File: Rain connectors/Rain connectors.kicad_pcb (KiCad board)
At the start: 2 copper layers, 22.7 x 25 mm, 8 parts, among them J1 Conn_01x06_Socket, J2 Conn_01x06_Socket, J3 Conn_01x03_Socket

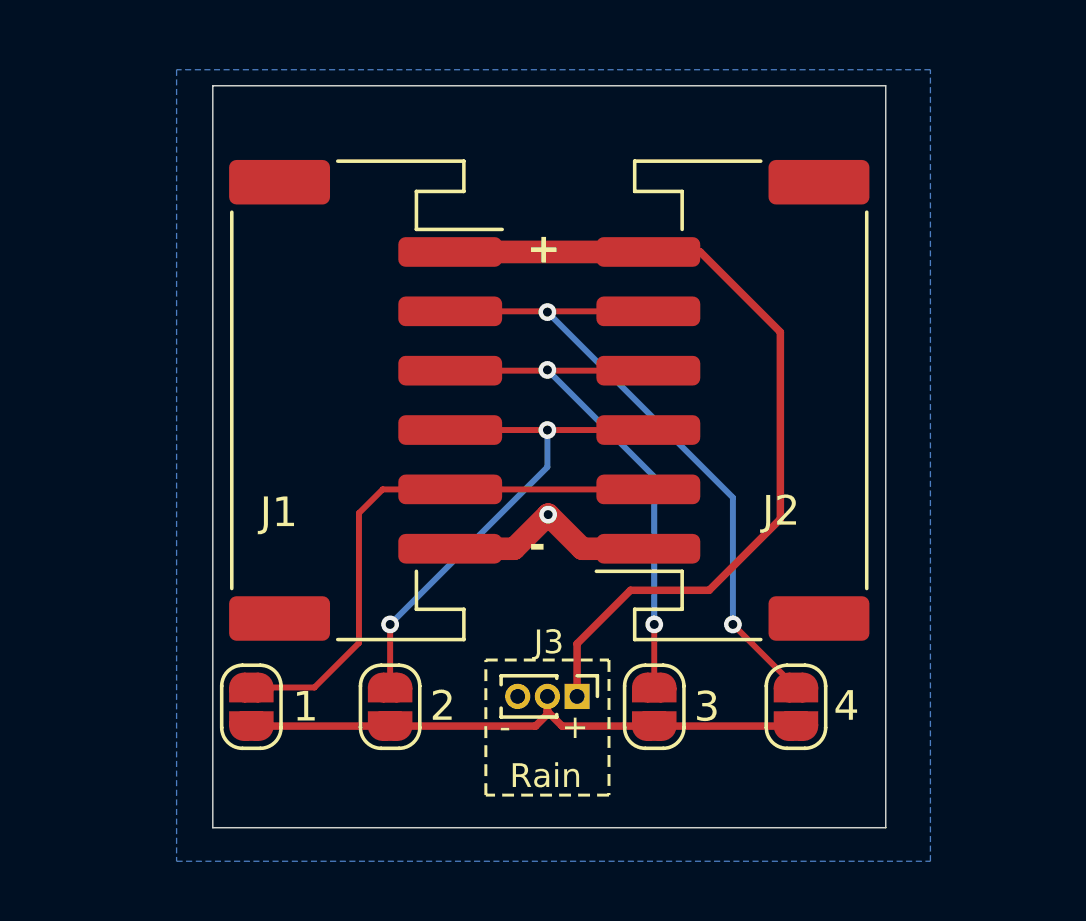
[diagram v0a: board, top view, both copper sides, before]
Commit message: Check to see if the rain connectors v.2. needs updating
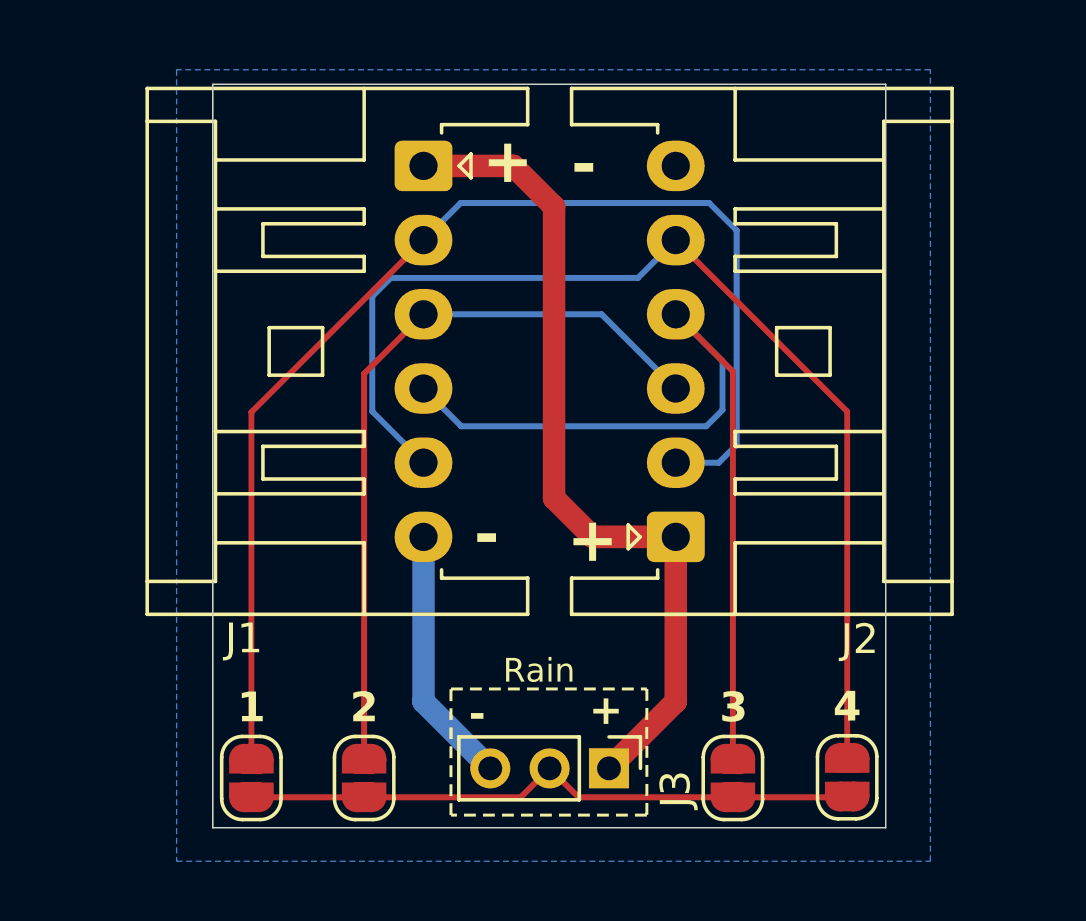
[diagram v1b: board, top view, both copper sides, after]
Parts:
- J1, J2: footprint Connector_JST:JST_PH_S6B-PH-SM4-TB_1x06-1MP_P2.00mm_Horizontal -> Connector_JST:JST_XA_S06B-XASK-1N-BN_1x06_P2.50mm_Horizontal
- J3: footprint Connector_PinHeader_1.00mm:PinHeader_1x03_P1.00mm_Vertical -> Connector_PinHeader_2.00mm:PinHeader_1x03_P2.00mm_Vertical
- moved J1 8.14 mm to (130.1, 74.2)
- moved J2 4.99 mm to (138.6, 86.7)
- moved REF** 4.93 mm to (134.4, 83.2)
- moved 3 3.58 mm to (140.5, 94.8)
- moved 4 2.94 mm to (144.4, 94.8)
- moved J3 2.65 mm to (136.3, 94.5)
- moved 2 2.55 mm to (128.1, 94.8)
- moved 1 2.40 mm to (124.3, 94.8)
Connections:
- 1 pad 2: Net-(J1-Pin_5) -> Net-(J1-Pin_2)
- 2 pad 2: Net-(J1-Pin_4) -> Net-(J1-Pin_3)
- 3 pad 2: Net-(J1-Pin_3) -> Net-(J1-Pin_4)
- 4 pad 2: Net-(J1-Pin_2) -> Net-(J1-Pin_5)
- J2 pad 1: GND -> +5V
- J2 pad 2: Net-(J1-Pin_5) -> Net-(J1-Pin_2)
- J2 pad 3: Net-(J1-Pin_4) -> Net-(J1-Pin_3)
- J2 pad 4: Net-(J1-Pin_3) -> Net-(J1-Pin_4)
- J2 pad 5: Net-(J1-Pin_2) -> Net-(J1-Pin_5)
- J2 pad 6: +5V -> GND
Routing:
- net Net-(J1-Pin_5): track 18.7 -> 37.2 mm
- net Net-(J1-Pin_2): track 22.8 -> 40.9 mm, vias 2 -> 0
- net Net-(J1-Pin_4): track 17.5 -> 30.5 mm, vias 2 -> 0
- net Net-(J1-Pin_3): track 18.9 -> 25.3 mm, vias 2 -> 0
- net GND: track 7.63 -> 8.73 mm, vias 1 -> 0
- net Net-(J3-Pin_2): track 19.9 -> 20.9 mm
- net +5V: track 28.9 -> 28.2 mm
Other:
- board text added: "330_Combined Sewer Tunnel Individual Rain Breakout Rev.2"
- board text removed: "330_Combined Sewer Tunnel Individual Rain Breakout Rev.1"

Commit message: Rev. 3
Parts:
- J1, J2: footprint Connector_JST:JST_XA_S06B-XASK-1N-BN_1x06_P2.50mm_Horizontal -> Connector_JST:JST_XA_S06B-XASK-1_1x06_P2.50mm_Horizontal
- moved REF** 3.48 mm to (134.6, 79.7)
- moved 4 2.59 mm to (146.4, 93.2)
- moved 1 2.59 mm to (122.2, 93.2)
- moved 3 1.97 mm to (141.7, 93.2)
- moved 2 1.87 mm to (127.1, 93.2)
- moved J3 0.92 mm to (136.6, 93.6)
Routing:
- net GND: track 8.73 -> 35.4 mm
- net Net-(J3-Pin_2): track 20.9 -> 25.6 mm
- net Net-(J1-Pin_2): track 40.9 -> 39.3 mm
- net Net-(J1-Pin_4): track 30.5 -> 29.2 mm
- net Net-(J1-Pin_5): track 37.2 -> 36.0 mm
- net +5V: track 28.2 -> 27.2 mm
- net Net-(J1-Pin_3): track 25.3 -> 24.8 mm
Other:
- board size 22.7 x 25 mm -> 26.8 x 24 mm
